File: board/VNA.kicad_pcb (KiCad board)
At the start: 2 copper layers, 100 x 100 mm, 132 parts, among them J1 Conn_02x05_Odd_Even, J10 Conn_01x01, J11 Conn_01x01, J12 Conn_01x01, J13 Barrel_Jack, J15 Conn_02x05_Odd_Even, J17 Conn_01x04, J18 Conn_01x01, J19 Conn_01x01, J2 Conn_Coaxial, J20 Conn_01x01, J21 Conn_01x01, J22 Conn_01x02, J3 Conn_01x01, J4 Conn_01x01, J5 Conn_01x01, J6 Conn_01x01, J7 Conn_01x01, J8 Conn_01x01, J9 Conn_Coaxial, Q1 SS9018, U1 SI5351A, U2 LM339, U3 SA612, U4 SA612, U5 SA612, U6 LM358, U7 LM358, U8 LM1117-3.3, U9 LM7805_TO220, Y1 27 MHz

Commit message: Turned a voltage regulator around
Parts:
- moved U9 4.22 mm to (145.6, 116.7), turned to 270 degrees
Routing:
- net Net-(C47-Pad1): track 47.0 -> 53.0 mm
- net +5V: track 320.0 -> 320.8 mm
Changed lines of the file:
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@@
     (links 254)
     (no_connects 0)
-    (area 48.252381 29.036639 153.343482 154.699701)
+    (area 49.924999 49.924999 150.075001 150.075001)
     (thickness 1.6)
     (drawings 37)
-    (tracks 1526)
+    (tracks 1535)
     (zones 0)
     (modules 132)
@@
   (layers
     (0 F.Cu signal)
-    (31 B.Cu signal)
+    (31 B.Cu signal hide)
     (32 B.Adhes user)
     (33 F.Adhes user)
@@
     (pad_to_mask_clearance 0.2)
     (aux_axis_origin 0 0)
-    (grid_origin 40.04564 49.6824)
     (visible_elements 7FFFFFFF)
     (pcbplotparams
@@
   )
   (module TO_SOT_Packages_THT:TO-220-3_Vertical (layer F.Cu)
-    (at 145.87728 120.9548 90)
+    (at 145.6436 116.7384 270)
     (descr "TO-220-3, Vertical, RM 2.54mm")
     (tags "TO-220-3 Vertical RM 2.54mm")
-    (fp_text reference U9 (at 2.54 -3.62 90) (layer F.SilkS)
+    (fp_text reference U9 (at 2.54 -3.62 270) (layer F.SilkS)
       (effects (font (size 1 1) (thickness 0.15)))
     )
-    (fp_text value LM7805_TO220 (at 2.54 3.92 90) (layer F.Fab)
+    (fp_text value LM7805_TO220 (at 2.54 3.92 270) (layer F.Fab)
       (effects (font (size 1 1) (thickness 0.15)))
     )
-    (fp_text user %R (at 2.54 -3.62 90) (layer F.Fab)
+    (fp_text user %R (at 2.54 -3.62 270) (layer F.Fab)
       (effects (font (size 1 1) (thickness 0.15)))
     )
@@
     (fp_line (start 7.79 2.16) (end 7.79 -2.75) (layer F.CrtYd) (width 0.05))
     (fp_line (start 7.79 -2.75) (end -2.71 -2.75) (layer F.CrtYd) (width 0.05))
-    (pad 1 thru_hole rect (at 0 0 90) (size 1.8 1.8) (drill 1) (layers *.Cu *.Mask)
+    (pad 1 thru_hole rect (at 0 0 270) (size 1.8 1.8) (drill 1) (layers *.Cu *.Mask)
       (net 55 "Net-(C47-Pad1)"))
-    (pad 2 thru_hole oval (at 2.54 0 90) (size 1.8 1.8) (drill 1) (layers *.Cu *.Mask)
+    (pad 2 thru_hole oval (at 2.54 0 270) (size 1.8 1.8) (drill 1) (layers *.Cu *.Mask)
       (net 2 GND))
-    (pad 3 thru_hole oval (at 5.08 0 90) (size 1.8 1.8) (drill 1) (layers *.Cu *.Mask)
+    (pad 3 thru_hole oval (at 5.08 0 270) (size 1.8 1.8) (drill 1) (layers *.Cu *.Mask)
       (net 45 +5V))
     (model ${KISYS3DMOD}/TO_SOT_Packages_THT.3dshapes/TO-220-3_Vertical.wrl
@@
     (effects (font (size 1 1) (thickness 0.15)))
   )
-  (gr_text LM7805 (at 144.1704 118.15064 90) (layer F.SilkS)
+  (gr_text LM7805 (at 147.6121 118.9736 90) (layer F.SilkS)
     (effects (font (size 1 1) (thickness 0.15)))
   )
@@
   (segment (start 88.773 115.951) (end 90.297 114.427) (width 0.35) (layer B.Cu) (net 44) (status 20))
   (segment (start 82.042 123.19) (end 82.042 122.936) (width 0.35) (layer B.Cu) (net 44) (status 30))
+  (segment (start 140.1572 123.4567) (end 140.7033 123.4567) (width 0.5) (layer B.Cu) (net 45))
+  (segment (start 142.7734 121.8565) (end 145.6436 121.8184) (width 0.5) (layer B.Cu) (net 45) (status 20))
+  (segment (start 140.7033 123.4567) (end 142.7734 121.8565) (width 0.5) (layer B.Cu) (net 45))
+  (segment (start 145.6436 121.8184) (end 148.0058 121.7168) (width 0.5) (layer F.Cu) (net 45) (status 10))
+  (segment (start 148.0058 121.7168) (end 148.69668 121.02592) (width 0.5) (layer F.Cu) (net 45))
+  (segment (start 137.922 119.43588) (end 137.922 119.4308) (width 0.5) (layer F.Cu) (net 45))
+  (via (at 137.922 119.43588) (size 0.6) (drill 0.4) (layers F.Cu B.Cu) (net 45))
+  (segment (start 148.806587 112.9792) (end 148.806587 112.979172) (width 0.5) (layer F.Cu) (net 45))
+  (segment (start 141.1224 112.9792) (end 148.806587 112.9792) (width 0.5) (layer F.Cu) (net 45))
+  (segment (start 138.9888 115.1128) (end 141.1224 112.9792) (width 0.5) (layer F.Cu) (net 45))
+  (segment (start 138.9888 118.364) (end 138.9888 115.1128) (width 0.5) (layer F.Cu) (net 45))
+  (segment (start 137.922 119.4308) (end 138.9888 118.364) (width 0.5) (layer F.Cu) (net 45))
   (segment (start 63.87084 136.5123) (end 64.42964 136.5123) (width 0.5) (layer F.Cu) (net 45))
   (segment (start 64.42964 136.5123) (end 67.743554 141.658908) (width 0.5) (layer F.Cu) (net 45))
@@
   (segment (start 63.94704 136.5123) (end 65.07734 135.382) (width 0.5) (layer B.Cu) (net 45))
   (segment (start 65.07734 135.382) (end 66.04 135.382) (width 0.5) (layer B.Cu) (net 45))
-  (segment (start 145.87728 115.8748) (end 145.02384 115.8748) (width 0.5) (layer B.Cu) (net 45) (status 30))
-  (segment (start 145.02384 115.8748) (end 142.1892 118.45544) (width 0.5) (layer B.Cu) (net 45) (status 10))
-  (segment (start 140.1953 123.4567) (end 139.2428 123.4567) (width 0.5) (layer B.Cu) (net 45))
-  (segment (start 142.1892 121.4628) (end 140.1953 123.4567) (width 0.5) (layer B.Cu) (net 45))
-  (segment (start 142.1892 118.45544) (end 142.1892 121.4628) (width 0.5) (layer B.Cu) (net 45))
+  (segment (start 140.1953 123.4567) (end 140.1572 123.4567) (width 0.5) (layer B.Cu) (net 45))
+  (segment (start 140.1572 123.4567) (end 139.2428 123.4567) (width 0.5) (layer B.Cu) (net 45))
   (segment (start 135.85444 118.2116) (end 135.85444 119.1768) (width 0.35) (layer B.Cu) (net 45))
   (segment (start 135.85444 119.1768) (end 136.42594 119.7483) (width 0.35) (layer B.Cu) (net 45))
@@
   (segment (start 137.922 119.1768) (end 138.4554 118.6434) (width 0.35) (layer B.Cu) (net 45))
   (segment (start 140.1064 78.4352) (end 138.6332 76.962) (width 0.5) (layer F.Cu) (net 45) (status 20))
-  (segment (start 147.2692 78.4352) (end 148.9964 79.9084) (width 0.5) (layer F.Cu) (net 45))
-  (segment (start 148.9964 79.9084) (end 148.9964 101.21646) (width 0.5) (layer F.Cu) (net 45))
+  (segment (start 148.9964 101.21646) (end 148.806587 112.979172) (width 0.5) (layer F.Cu) (net 45))
   (segment (start 140.1064 78.4352) (end 147.2692 78.4352) (width 0.5) (layer F.Cu) (net 45))
+  (segment (start 148.9964 79.9084) (end 148.9964 101.21646) (width 0.5) (layer F.Cu) (net 45))
+  (segment (start 147.2692 78.4352) (end 148.9964 79.9084) (width 0.5) (layer F.Cu) (net 45))
   (segment (start 137.922 119.43588) (end 137.234613 119.732542) (width 0.5) (layer B.Cu) (net 45))
-  (segment (start 137.922 119.43588) (end 140.04036 119.4054) (width 0.5) (layer F.Cu) (net 45))
-  (via (at 137.922 119.43588) (size 0.6) (drill 0.4) (layers F.Cu B.Cu) (net 45))
-  (segment (start 145.87728 115.8748) (end 140.04036 119.4054) (width 0.5) (layer F.Cu) (net 45) (status 10))
   (segment (start 101.3841 119.7483) (end 99.568 117.9322) (width 0.5) (layer B.Cu) (net 45))
   (segment (start 136.6266 119.7483) (end 136.42594 119.7483) (width 0.5) (layer B.Cu) (net 45))
@@
   (segment (start 138.6459 138.7729) (end 139.6111 138.7729) (width 0.5) (layer F.Cu) (net 45) (status 10))
   (segment (start 148.69668 116.95684) (end 148.7424 116.95684) (width 0.5) (layer F.Cu) (net 45))
-  (segment (start 148.69668 139.52982) (end 148.69668 116.95684) (width 0.5) (layer F.Cu) (net 45))
+  (segment (start 148.69668 139.52982) (end 148.69668 121.02592) (width 0.5) (layer F.Cu) (net 45))
+  (segment (start 148.69668 121.02592) (end 148.69668 116.95684) (width 0.5) (layer F.Cu) (net 45))
   (segment (start 147.5232 140.7033) (end 148.69668 139.52982) (width 0.5) (layer F.Cu) (net 45))
   (segment (start 141.5415 140.7033) (end 147.5232 140.7033) (width 0.5) (layer F.Cu) (net 45))
   (segment (start 139.6111 138.7729) (end 141.5415 140.7033) (width 0.5) (layer F.Cu) (net 45))
   (segment (start 99.568 114.3) (end 99.568 117.9322) (width 0.5) (layer B.Cu) (net 45) (status 10))
-  (segment (start 145.43532 115.66906) (end 146.21256 115.84432) (width 0.5) (layer B.Cu) (net 45) (status 30))
-  (segment (start 145.87728 115.8748) (end 147.81276 115.6716) (width 0.5) (layer F.Cu) (net 45) (status 10))
-  (segment (start 147.81276 115.6716) (end 148.7424 117.27434) (width 0.5) (layer F.Cu) (net 45))
-  (segment (start 148.9964 101.21646) (end 148.7424 116.95684) (width 0.5) (layer F.Cu) (net 45))
+  (segment (start 148.806587 112.979172) (end 148.7424 116.95684) (width 0.5) (layer F.Cu) (net 45))
   (segment (start 148.7424 116.95684) (end 148.7424 117.27434) (width 0.5) (layer F.Cu) (net 45))
   (segment (start 99.568 114.3) (end 99.568 114.681) (width 0.35) (layer B.Cu) (net 45) (status 30))
@@
   (segment (start 71.07936 115.3033) (end 71.07936 115.71798) (width 0.25) (layer F.Cu) (net 54) (status 30))
   (segment (start 76.032 112.268) (end 75.271741 112.252701) (width 0.25) (layer F.Cu) (net 54) (status 10))
+  (segment (start 145.6436 116.7384) (end 145.1102 116.7384) (width 0.5) (layer F.Cu) (net 55) (status 30))
+  (segment (start 145.1102 116.7384) (end 143.764 118.6688) (width 0.5) (layer F.Cu) (net 55) (status 10))
+  (segment (start 143.764 118.6688) (end 143.764 125.1458) (width 0.5) (layer F.Cu) (net 55))
+  (segment (start 143.764 125.1458) (end 145.3896 128.524) (width 0.5) (layer F.Cu) (net 55))
+  (segment (start 145.3896 128.524) (end 145.3896 131.9276) (width 0.5) (layer F.Cu) (net 55))
   (segment (start 145.87728 131.43992) (end 145.3896 131.9276) (width 0.5) (layer F.Cu) (net 55))
-  (segment (start 145.87728 120.9548) (end 145.87728 131.43992) (width 0.5) (layer F.Cu) (net 55) (status 10))
   (segment (start 135.3312 131.3688) (end 135.3312 139.5984) (width 0.5) (layer B.Cu) (net 55))
   (segment (start 137.0457 141.3129) (end 138.6459 141.3129) (width 0.5) (layer B.Cu) (net 55) (status 20))

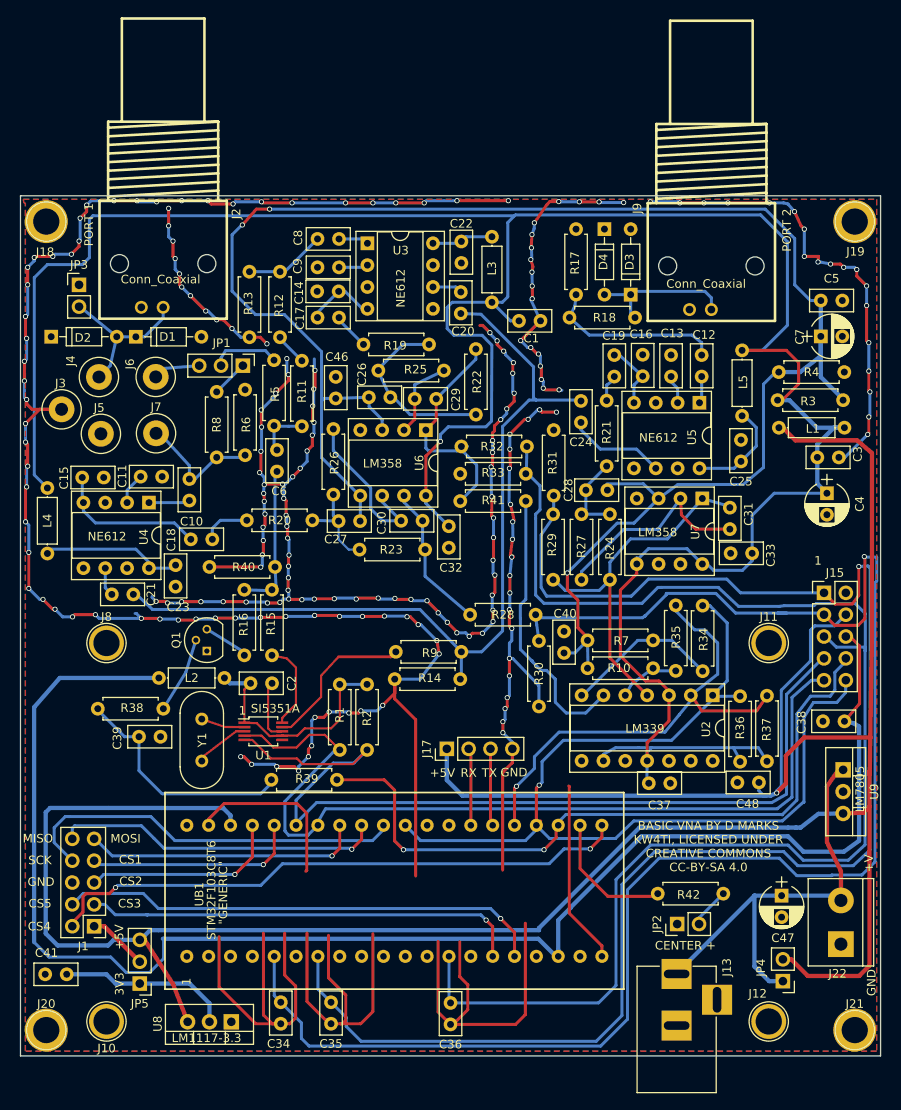
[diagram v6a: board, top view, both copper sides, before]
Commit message: Increased isolation between ports
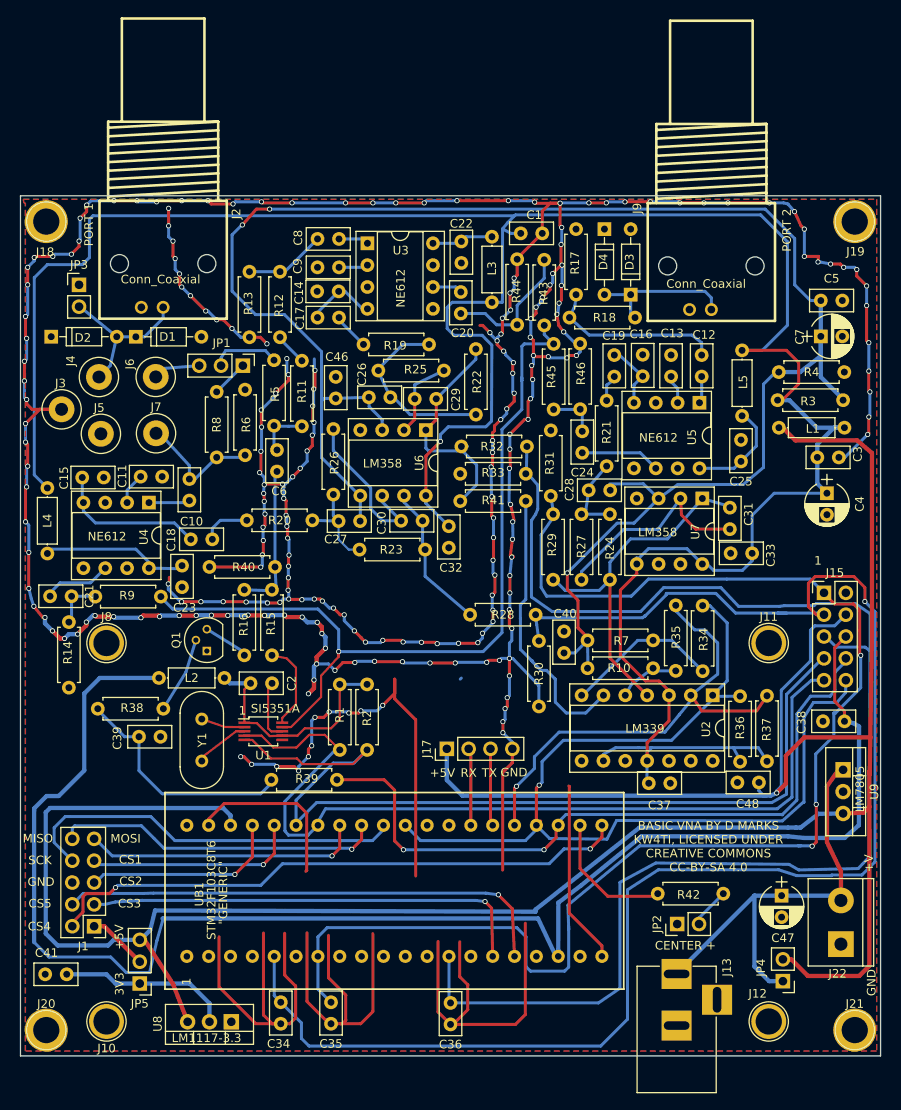
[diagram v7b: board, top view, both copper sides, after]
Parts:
- added R43: 1.5k, Resistors_THT:R_Axial_DIN0207_L6.3mm_D2.5mm_P7.62mm_Horizontal, F.Cu at (110.9, 57.4)
- added R44: 51R, Resistors_THT:R_Axial_DIN0207_L6.3mm_D2.5mm_P7.62mm_Horizontal, F.Cu at (107.7, 57.4)
- added R45: 1.5k, Resistors_THT:R_Axial_DIN0207_L6.3mm_D2.5mm_P7.62mm_Horizontal, F.Cu at (112.0, 74.8)
- added R46: 51R, Resistors_THT:R_Axial_DIN0207_L6.3mm_D2.5mm_P7.62mm_Horizontal, F.Cu at (115.1, 67.2)
- moved R9 43.0 mm to (58.7, 96.6), turned to 0 degrees
- moved R14 37.9 mm to (55.6, 107.2), turned to 90 degrees
- moved C1 10.2 mm to (108.2, 54.4)
- moved C21 7.18 mm to (53.4, 96.6)
- moved C24 3.53 mm to (115.3, 79.9)
- moved C23 0.75 mm to (68.8, 95.5)
- moved R31 0.33 mm to (111.7, 77.3)
- moved C28 0.33 mm to (116.1, 84.2)
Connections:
- C20 pad 2: CLK1 -> CLK1B
- C21 pad 2: CLK1 -> CLK1A
- C24 pad 2: CLK1 -> CLK1C
- R14 pad 2: CLK1 -> CLK1A
- R9 pad 1: CLK1 -> CLK1A
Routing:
- net CLK1: track 99.1 -> 0.00 mm
- net Net-(R43-Pad2): track 18.3 -> 97.8 mm, vias 0 -> 1
- net (no net): track 0.00 -> 50.7 mm, vias 0 -> 11
- net DEMODCUR2: track 181.4 -> 164.1 mm, vias 1 -> 3
- net CLK1B: track 0.00 -> 16.0 mm
- net DEMODCUR: track 187.3 -> 180.7 mm
- net CLK1A: track 0.00 -> 5.92 mm
- net CLK1C: track 0.00 -> 5.82 mm
- net GND: track 709.1 -> 713.8 mm, vias 206 -> 217
- net Net-(C21-Pad1): track 3.36 -> 8.00 mm
- net Net-(C24-Pad1): track 11.4 -> 9.30 mm
- net FILT5V: track 312.4 -> 310.5 mm
- net DEMODVOLT: track 163.1 -> 164.9 mm
- net PB10: track 51.0 -> 52.3 mm
- net PB11: track 56.6 -> 57.9 mm
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
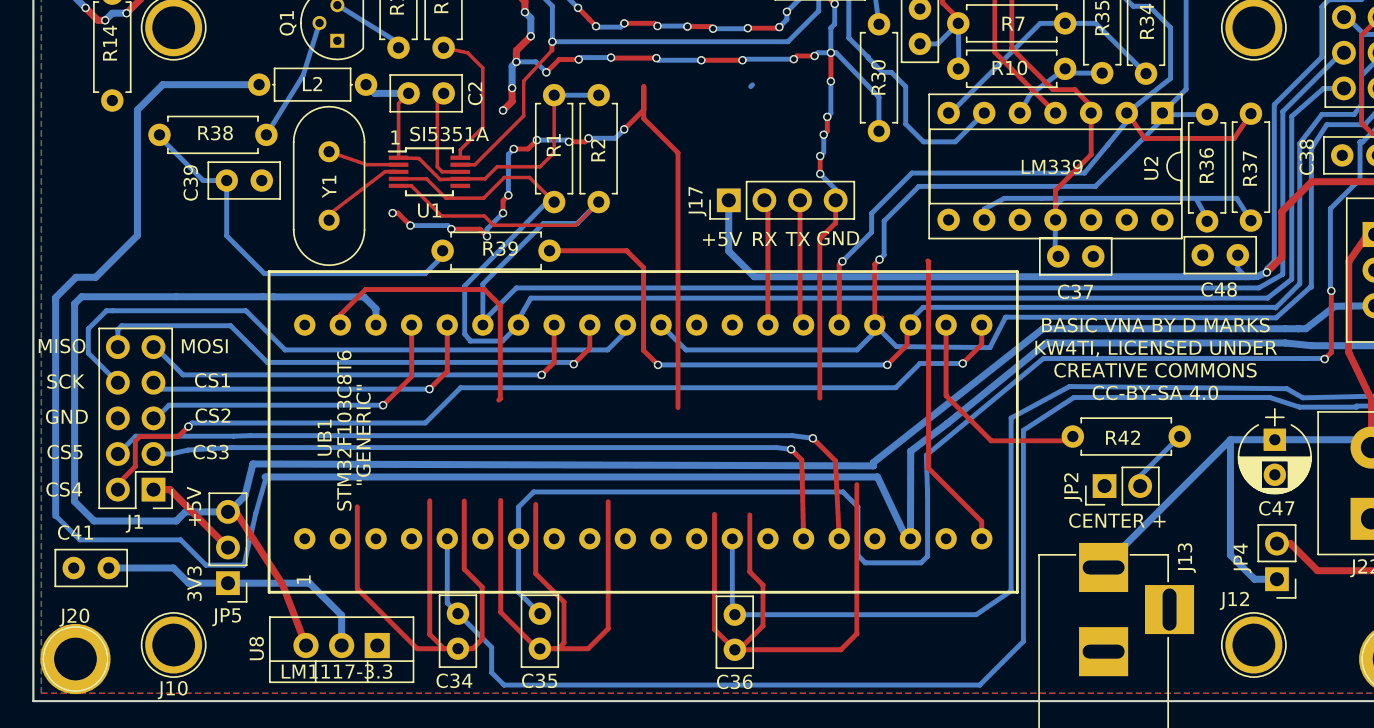
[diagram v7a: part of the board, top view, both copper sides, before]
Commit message: Added extra outputs to connector, changed display off pin
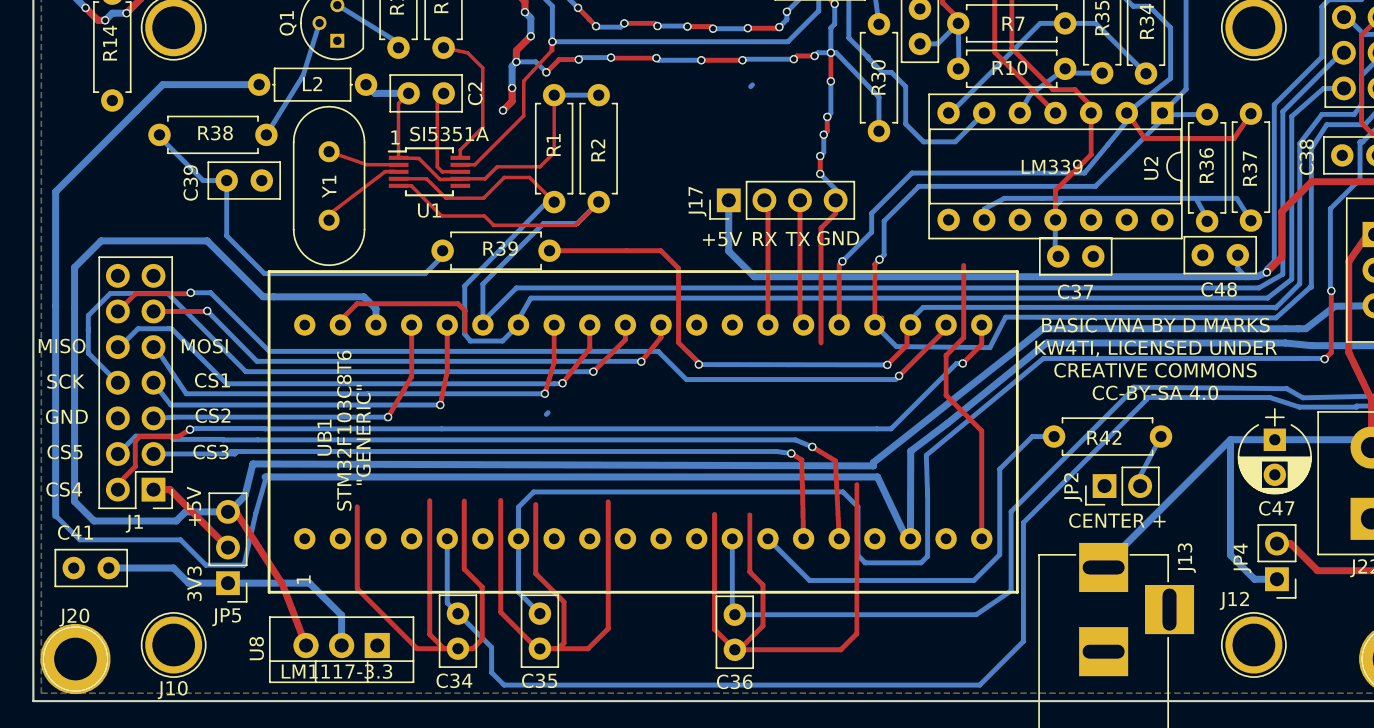
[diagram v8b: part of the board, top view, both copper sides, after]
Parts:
- J1: value Conn_02x05_Odd_Even -> Conn_02x07_Odd_Even; footprint Pin_Headers:Pin_Header_Straight_2x05_Pitch2.54mm -> Pin_Headers:Pin_Header_Straight_2x07_Pitch2.54mm
- moved R42 1.34 mm to (130.4, 131.1)
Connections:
- UB1 pad 19: (no net) -> Net-(R42-Pad2)
- UB1 pad 26: Net-(R42-Pad2) -> Net-(J1-Pad12)
- UB1 pad 38: SYNCSAMPLE -> Net-(J1-Pad11)
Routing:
- net Net-(J1-Pad12): track 0.00 -> 63.9 mm, vias 0 -> 2
- net (no net): track 50.7 -> 0.36 mm, vias 11 -> 0
- net Net-(J1-Pad11): track 0.00 -> 39.4 mm, vias 0 -> 2
- net SYNCSAMPLE: track 117.5 -> 101.0 mm
- net Net-(R42-Pad2): track 15.5 -> 29.9 mm
- net GND: track 713.8 -> 700.8 mm
- net +5V: track 321.1 -> 325.9 mm
- net Net-(J1-Pad8): track 45.8 -> 49.6 mm, vias 0 -> 1
- net DEMODCUR: track 180.7 -> 177.2 mm
- net DEMODVOLT: track 164.9 -> 161.4 mm
- net Net-(J1-Pad9): track 32.6 -> 34.7 mm
- net Net-(J1-Pad7): track 25.0 -> 27.0 mm
- net +3V3: track 181.9 -> 181.1 mm
- net Net-(JP2-Pad2): track 4.70 -> 3.90 mm
- net PB10: track 52.3 -> 53.0 mm
